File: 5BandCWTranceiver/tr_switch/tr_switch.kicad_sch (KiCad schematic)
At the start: 44 parts, among them J1 Conn_01x02, J10 Conn_01x02_Male, J11 Conn_01x02_Male, J12 Conn_01x02_Male, J2 Conn_01x02, J3 Conn_01x02, J4 Conn_Coaxial, J5 Conn_01x02, J6 Conn_Coaxial, J7 Conn_Coaxial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

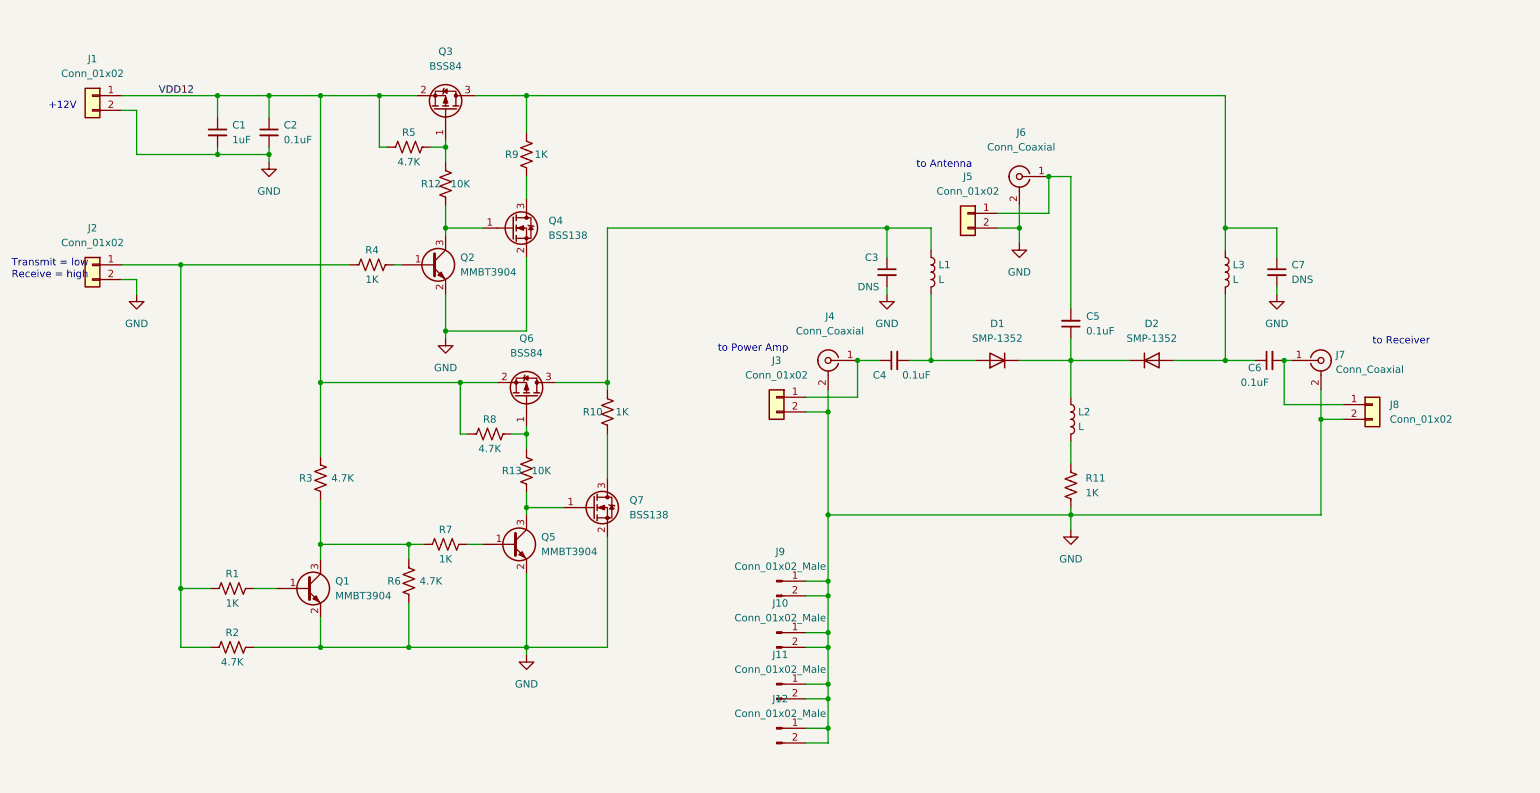
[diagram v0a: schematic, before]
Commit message: Updated schematics and layout
Updated T/R switch to rev. B after lab tests
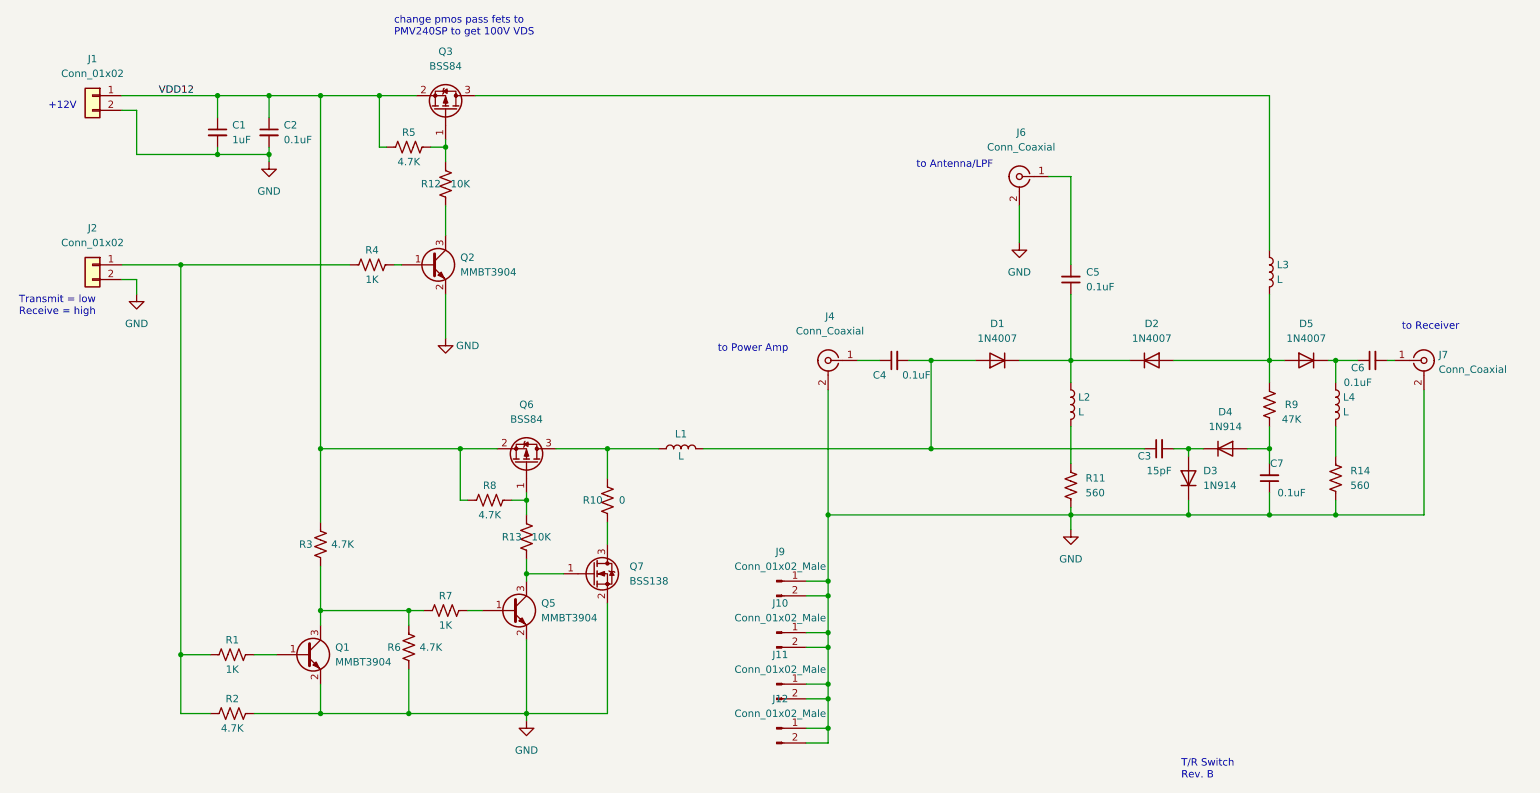
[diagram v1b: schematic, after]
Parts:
- removed J3, J5, J8: Conn_01x02, Connector_PinHeader_2.54mm:PinHeader_1x02_P2.54mm_Vertical, symbol Connector_Generic:Conn_01x02
- removed Q4: BSS138, Package_TO_SOT_SMD:SOT-23, symbol Device:Q_NMOS_GSD
- added D3, D4: 1N914, Diode_THT:D_DO-35_SOD27_P7.62mm_Horizontal, symbol Device:D
- added D5: 1N4007, Diode_THT:D_DO-41_SOD81_P10.16mm_Horizontal, symbol Device:D
- added L4: L, Inductor_THT:L_Toroid_Vertical_L10.0mm_W5.0mm_P5.08mm, symbol Device:L
- added R14: 560, Resistor_THT:R_Axial_DIN0411_L9.9mm_D3.6mm_P15.24mm_Horizontal, symbol Device:R_US
- C3: value DNS -> 15pF; footprint Capacitor_SMD:C_0603_1608Metric_Pad1.08x0.95mm_HandSolder -> Capacitor_THT:C_Disc_D5.0mm_W2.5mm_P5.00mm
- C7: value DNS -> 0.1uF; footprint Capacitor_SMD:C_0603_1608Metric_Pad1.08x0.95mm_HandSolder -> Capacitor_THT:C_Disc_D5.0mm_W2.5mm_P5.00mm
- D1, D2: value SMP-1352 -> 1N4007; footprint Diode_SMD:D_SC-80_HandSoldering -> Diode_THT:D_DO-41_SOD81_P10.16mm_Horizontal
- R10: value 1K -> 0
- R11: value 1K -> 560; footprint Resistor_SMD:R_0603_1608Metric_Pad0.98x0.95mm_HandSolder -> Resistor_THT:R_Axial_DIN0411_L9.9mm_D3.6mm_P15.24mm_Horizontal
- R9: value 1K -> 47K
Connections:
- net GND: now also C7.1, D3.1 (K), R14.2; no longer C3.2, C7.2
- net at D2.2 (A), L3.2: now also R9.2, D5.2 (A); no longer C6.1
- net at C4.2, D1.2 (A), L1.2: now also C3.1
- net at R9.1: now also C7.2, D4.2 (A)
- net at L1.1, Q6.3 (D), R10.2: no longer C3.1
- net at L3.1, Q3.3 (D): no longer C7.1, R9.2
- new net: C3.2, D3.2 (A), D4.1 (K)
- new net: L4.2, R14.1
- new net: C6.1, D5.1 (K), L4.1
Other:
- note added: "T/R Switch Rev. B"
- note added: "change pmos pass fets to PMV240SP to get 100V VDS"
- note added: "to Antenna/LPF"
- note removed: "to Antenna"
- moved on the sheet: C5, C6, J7, L1, L2, L3, Q1, Q5, Q6, Q7, R1, R10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
